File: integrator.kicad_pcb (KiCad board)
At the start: 4 copper layers, 65.5 x 117 mm, 87 parts, among them J1 SJ-3524-SMT, J2 SJ-3524-SMT, J5 USB4105-GF-A, J6 Conn_ARM_JTAG_SWD_10, J7 test point, SW1 EVQP40B3M, SW2 EVQP40B3M, SW3 EVQP40B3M, SW4 436333033816, U1 MCP1501T-30E_RW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

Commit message: bugfixes on v6
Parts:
- added C34: 0.1uf, Capacitor_SMD:C_0805_2012Metric, B.Cu at (143.2, 62.5)
- added G***: LOGO, misc:glutenfrei, F.Cu at (163.4, 135.2)
- added G***: LOGO, misc:UKCA logo, F.Cu at (153.1, 127.0)
- added JP10: Jumper, Jumper:SolderJumper-2_P1.3mm_Bridged2Bar_Pad1.0x1.5mm, B.Cu at (176.1, 129.5)
- added JP11: Jumper, Jumper:SolderJumper-2_P1.3mm_Bridged2Bar_Pad1.0x1.5mm, B.Cu at (132.9, 149.9)
- added JP9: Jumper, Jumper:SolderJumper-2_P1.3mm_Bridged2Bar_Pad1.0x1.5mm, B.Cu at (136.9, 151.9)
- added REF**: FCC-Logo_7.3x6mm_SilkScreen, Symbol:FCC-Logo_7.3x6mm_SilkScreen, F.Cu at (152.9, 117.7)
- added REF**: CE-Logo_8.5x6mm_SilkScreen, Symbol:CE-Logo_8.5x6mm_SilkScreen, F.Cu at (163.7, 122.2)
- C11, C12: footprint Capacitor_SMD:C_0805_2012Metric -> Capacitor_SMD:C_0603_1608Metric
- U1: footprint misc:MCP1501T-18E_RW -> Package_SO:SOIC-8-1EP_3.9x4.9mm_P1.27mm_EP2.29x3mm_ThermalVias
- moved C3 3.63 mm to (167.0, 137.8), turned to 270 degrees
- moved U1 1.94 mm to (167.6, 143.0)
- moved JP6 1.30 mm to (163.9, 145.0)
- moved C10 0.20 mm to (166.6, 99.6)
- moved C14 0.20 mm to (178.0, 99.6)
- moved C33 0.20 mm to (171.8, 99.6)
- moved C6 0.20 mm to (160.6, 99.6)
- moved R20 0.20 mm to (176.0, 99.6)
- moved R8 0.20 mm to (173.8, 99.6)
- moved R9 0.20 mm to (162.6, 99.6)
- moved R5 0.20 mm to (164.6, 99.6)
- moved C16 0.12 mm to (177.1, 154.9)
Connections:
- C15 pad 1: VRaw -> Net-(C15-Pad1)
- C16 pad 1: (no net) -> Net-(C16-Pad1)
- C16 pad 2: Earth -> Net-(C16-Pad2)
- J1 pad 4: (no net) -> Net-(J1-Pad4)
- J2 pad 4: (no net) -> Net-(J2-Pad4)
- J5 pad A8: (no net) -> Net-(J5-PadA8)
- J5 pad B8: (no net) -> Net-(J5-PadB8)
- J6 pad 6: (no net) -> Net-(J6-Pad6)
- J6 pad 7: (no net) -> Net-(J6-Pad7)
- J6 pad 8: (no net) -> Net-(J6-Pad8)
- J6 pad 9: (no net) -> Net-(J6-Pad9)
- POGO1 pad 1: (no net) -> Net-(POGO1-Pad1)
- POGO1 pad 2: (no net) -> Net-(POGO1-Pad2)
- POGO1 pad 4: (no net) -> Net-(POGO1-Pad4)
- POGO1 pad 8: (no net) -> Net-(POGO1-Pad8)
- SW4 pad 1: sw4 -> Net-(JP9-Pad2)
- SW4 pad 3: (no net) -> Net-(JP10-Pad2)
- U2 pad 7: (no net) -> Net-(U2-Pad7)
- U2 pad 8: (no net) -> Net-(U2-Pad8)
- U3 pad 10: (no net) -> Net-(U3-Pad10)
- U3 pad 11: (no net) -> Net-(U3-Pad11)
- U3 pad 9: (no net) -> Net-(U3-Pad9)
- U5 pad 16: spi_clock -> spi_cs
- U5 pad 17: spi_cs -> spi_clock
- U5 pad 27: (no net) -> Net-(U5-Pad27)
- U5 pad 28: (no net) -> Net-(U5-Pad28)
- U5 pad 37: (no net) -> Net-(U5-Pad37)
- U5 pad 39: (no net) -> Net-(U5-Pad39)
- U5 pad 40: (no net) -> Net-(U5-Pad40)
- U5 pad 41: (no net) -> Net-(U5-Pad41)
- U5 pad 9: (no net) -> Net-(U5-Pad9)
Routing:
- net Net-(JP10-Pad2): track 0.00 -> 63.4 mm, vias 0 -> 2
- net sw4: track 40.7 -> 29.7 mm
- net AGnd: track 44.7 -> 55.1 mm, vias 7 -> 6
- net Net-(JP9-Pad2): track 0.00 -> 8.68 mm
- net (no net): track 5.96 -> 0.00 mm
- net Net-(C15-Pad1): track 0.00 -> 5.15 mm
- net Net-(C16-Pad1): track 0.00 -> 4.43 mm
- net Net-(C16-Pad2): track 0.00 -> 3.18 mm, vias 0 -> 1
- net spi_cs: track 42.8 -> 45.0 mm, vias 0 -> 2
- net Earth: track 111.5 -> 113.7 mm, vias 57 -> 55
- net /po_batt: track 110.9 -> 112.8 mm, vias 3 -> 4
- net VReg: track 273.2 -> 274.5 mm
- net VRaw: track 78.3 -> 79.3 mm
- net ring2_out: track 80.2 -> 80.8 mm
- net Net-(U3-Pad11): track 0.00 -> 0.53 mm

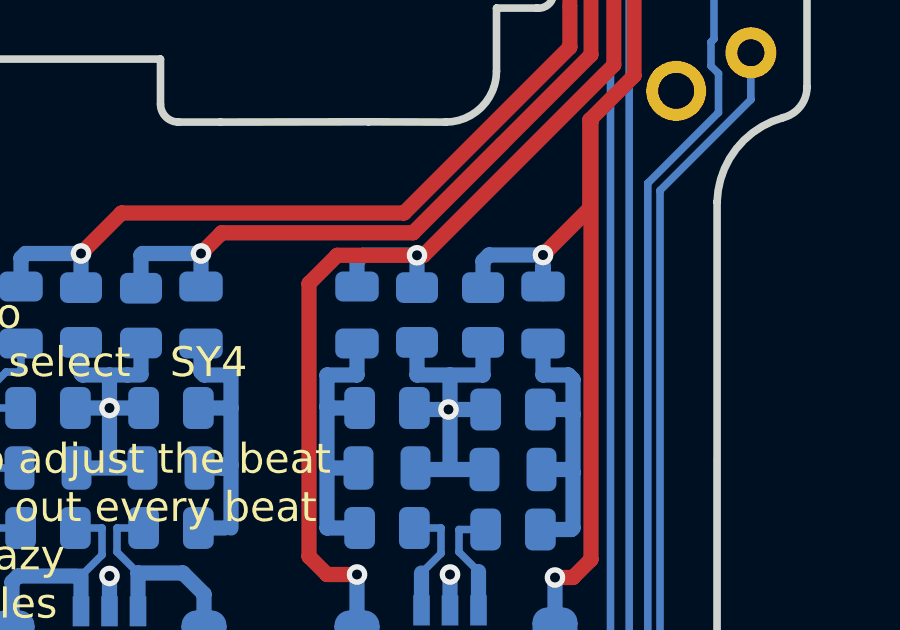
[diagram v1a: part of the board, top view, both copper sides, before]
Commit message: adj popcorn spacing
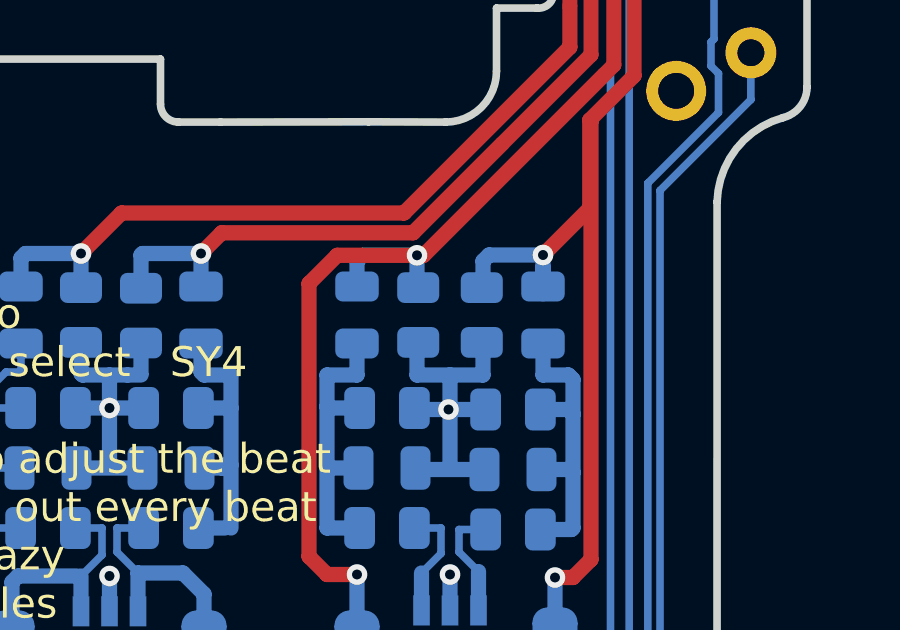
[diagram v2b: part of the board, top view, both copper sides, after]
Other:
- board text added: "*"
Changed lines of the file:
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@@
   (general
     (thickness 1.6002)
-    (drawings 521)
+    (drawings 522)
     (tracks 1316)
     (zones 0)
@@
     (0 Front signal)
     (1 In1.Cu signal)
-    (2 In2.Cu signal)
+    (2 In2.Cu signal hide)
     (31 Back signal)
     (34 B.Paste user)
@@
       (effects (font (size 1 1) (thickness 0.15)) (justify mirror))
     )
-    (fp_text user %R (at 0 0 90) (layer B.Fab)
-      (effects (font (size 0.98 0.98) (thickness 0.15)) (justify mirror))
-    )
     (fp_line (start 0 -2.56) (end 1.95 -2.56) (layer B.SilkS) (width 0.12))
     (fp_line (start 0 -2.56) (end -1.95 -2.56) (layer B.SilkS) (width 0.12))
@@
     (fp_line (start 3.7 -2.7) (end 3.7 2.7) (layer B.CrtYd) (width 0.05))
     (fp_line (start 3.7 2.7) (end -3.7 2.7) (layer B.CrtYd) (width 0.05))
+    (fp_text user %R (at 0 0 90) (layer B.Fab)
+      (effects (font (size 0.98 0.98) (thickness 0.15)) (justify mirror))
+    )
+    (fp_text user * (at 0 0 90) (layer B.SilkS)
+      (effects (font (size 1.016 1.016) (thickness 0.1524)) (justify mirror))
+    )
     (pad "" smd roundrect (at 0.57 -0.75 90) (size 0.96 1.25) (layers B.Paste) (roundrect_rratio 0.25))
     (pad "" smd roundrect (at 0.57 0.75 90) (size 0.96 1.25) (layers B.Paste) (roundrect_rratio 0.25))
@@
     (tags LED)
     (attr smd)
-    (fp_text reference LED4 (at 2.35 0.4) (layer B.SilkS)
+    (fp_text reference LED4 (at 1.95 0.4) (layer B.SilkS)
       (effects (font (size 1 1) (thickness 0.15)) (justify mirror))
     )
@@
   )
   (module Resistor_SMD:R_0805_2012Metric (layer Back)
-    (at 175.999 99.6 90)
+    (at 175.959 99.6 90)
     (descr "Resistor SMD 0805 (2012 Metric), square (rectangular) end terminal, IPC_7351 nominal, (Body size source: IPC-SM-782 page 72, https://www.pcb-3d.com/wordpress/wp-content/uploads/ipc-sm-782a_amendment_1_and_2.pdf), generated with kicad-footprint-generator")
     (tags resistor)
@@
   )
   (module Resistor_SMD:R_0805_2012Metric (layer Back)
-    (at 173.799 99.6 90)
+    (at 173.839 99.6 90)
     (descr "Resistor SMD 0805 (2012 Metric), square (rectangular) end terminal, IPC_7351 nominal, (Body size source: IPC-SM-782 page 72, https://www.pcb-3d.com/wordpress/wp-content/uploads/ipc-sm-782a_amendment_1_and_2.pdf), generated with kicad-footprint-generator")
     (tags resistor)
@@
     (tags inductor)
     (attr smd)
-    (fp_text reference L1 (at -0.1 -1.6 90) (layer B.SilkS)
+    (fp_text reference L1 (at -1.55 -1.5) (layer B.SilkS)
       (effects (font (size 1 1) (thickness 0.15)) (justify mirror))
     )
@@
     )
   )
+  (gr_text * (at 169.649 147.25) (layer B.SilkS)
+    (effects (font (size 0.762 0.762) (thickness 0.1905)))
+  )
   (gr_line (start 182.399 129.75) (end 175.649 126.65) (layer F.SilkS) (width 0.25))

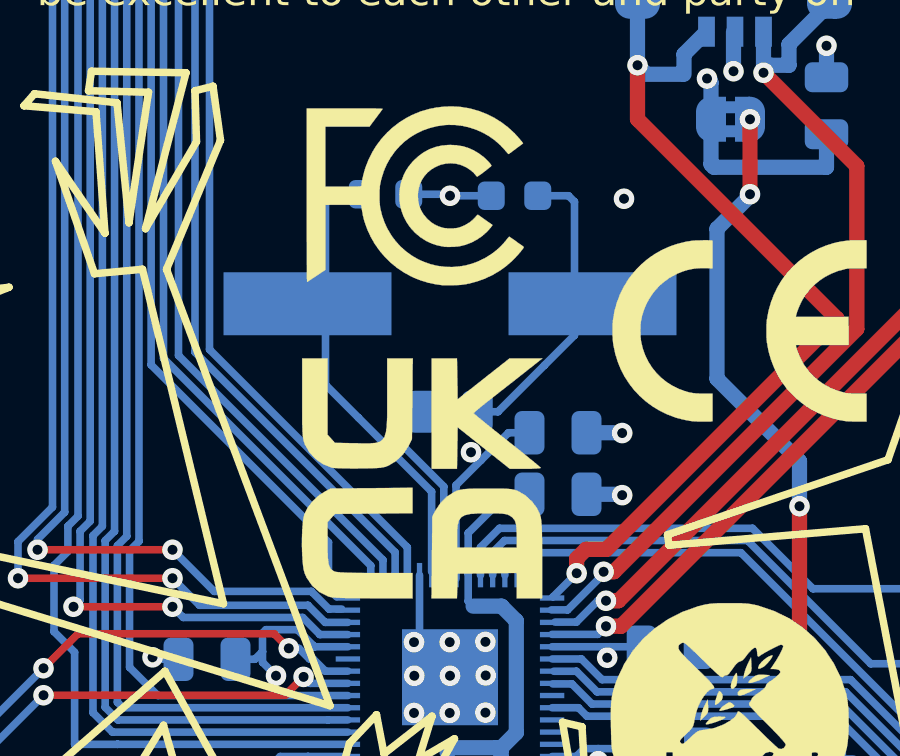
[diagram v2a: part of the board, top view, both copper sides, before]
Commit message: changing to ABM10-166-12.000MHZ-T3 crystal
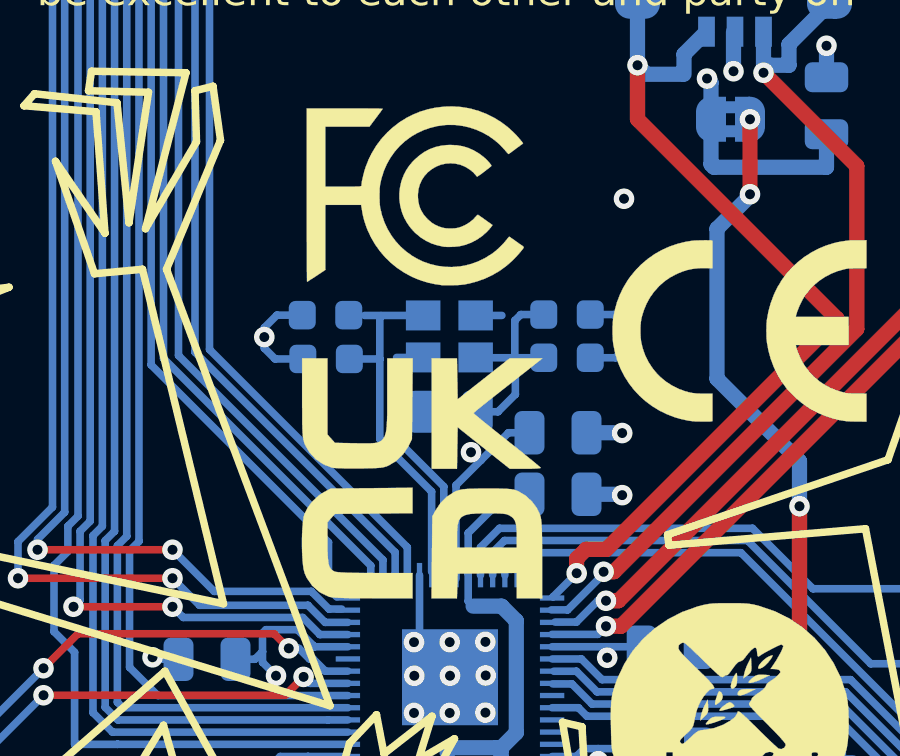
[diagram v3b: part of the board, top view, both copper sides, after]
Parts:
- added C++: 27pf, Capacitor_SMD:C_0603_1608Metric, B.Cu at (149.9, 123.1)
- added C++: 27pf, Capacitor_SMD:C_0603_1608Metric, B.Cu at (157.9, 121.6)
- Y1: footprint misc:XTAL_ABLS-12.000MHZ-B4-T -> Crystal:Crystal_SMD_2520-4Pin_2.5x2.0mm
- moved C11 5.68 mm to (157.9, 123.0), turned to 0 degrees
- moved C12 4.50 mm to (149.9, 121.6), turned to 0 degrees
- moved Y1 1.09 mm to (154.0, 122.3)
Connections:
- Y1 pad 2: Net-(C11-Pad1) -> (no net)
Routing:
- net /xin: track 17.3 -> 12.3 mm
- net Earth: track 113.7 -> 118.2 mm, vias 55 -> 56
- net Net-(C11-Pad1): track 11.5 -> 7.22 mm
- net (no net): track 0.00 -> 1.76 mm

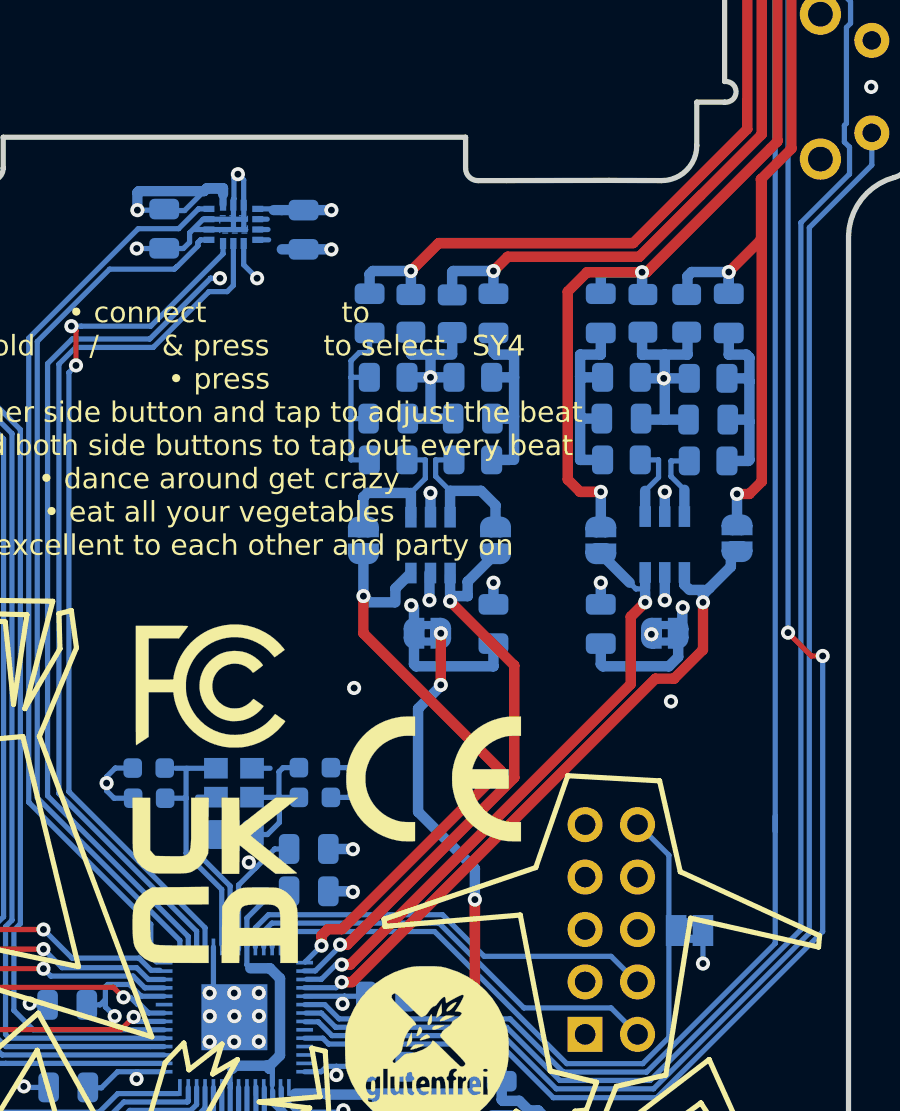
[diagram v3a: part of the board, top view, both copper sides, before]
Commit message: repositioned audio output stage
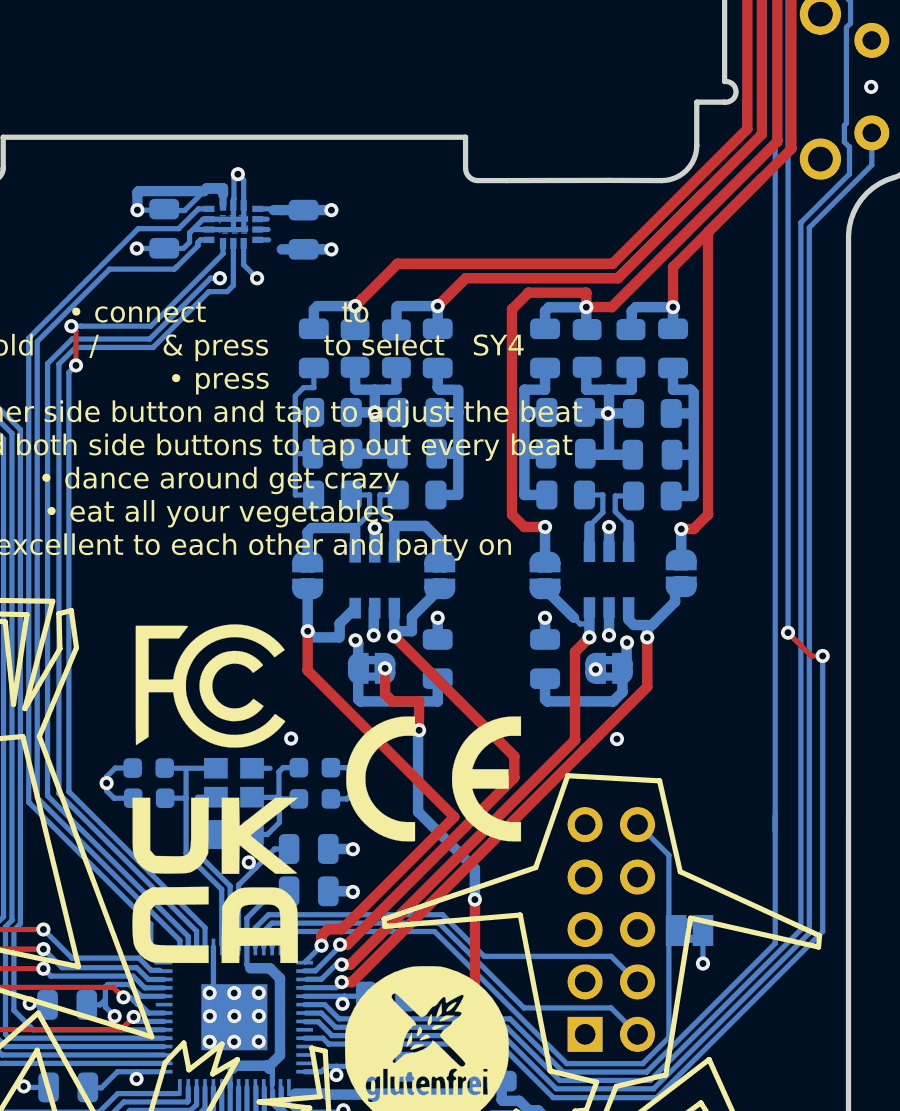
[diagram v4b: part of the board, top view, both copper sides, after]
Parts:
- removed C++ (x2): 27pf, Capacitor_SMD:C_0603_1608Metric
- added C11: 6pf, Capacitor_SMD:C_0603_1608Metric, B.Cu at (149.9, 123.1)
- added C11: 6pf, Capacitor_SMD:C_0603_1608Metric, B.Cu at (157.9, 121.6)
- C11, C12: value 27pf -> 6pf
- moved C33 3.19 mm to (169.1, 101.3)
- moved C8 3.19 mm to (170.1, 106.4)
- moved JP2 3.19 mm to (164.0, 112.3)
- moved JP3 3.19 mm to (157.6, 112.3)
- moved JP5 3.19 mm to (169.1, 112.3)
- moved R17 3.19 mm to (170.1, 104.4)
- moved R19 3.19 mm to (170.1, 108.4)
- moved R20 3.19 mm to (173.3, 101.3)
- moved U4 3.19 mm to (160.8, 112.5)
- moved C32 3.19 mm to (169.1, 116.3)
- moved C10 3.19 mm to (163.9, 101.3)
- moved C13 3.19 mm to (162.9, 106.4)
- moved C14 3.19 mm to (175.3, 101.3)
- moved C17 3.19 mm to (158.8, 106.4)
- moved C6 3.19 mm to (157.9, 101.3)
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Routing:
- net tip2_out: track 73.6 -> 79.2 mm
- net ring2_out: track 80.8 -> 85.7 mm
- net tip2: track 32.7 -> 29.4 mm
- net tip1_out: track 96.6 -> 100.0 mm
- net ring1_out: track 100.2 -> 103.4 mm
- net ring2: track 30.1 -> 27.3 mm
- net ring1: track 30.1 -> 27.7 mm
- net Earth: track 118.2 -> 119.4 mm
- net VAref: track 55.2 -> 54.5 mm
- net tip1: track 28.8 -> 28.2 mm
